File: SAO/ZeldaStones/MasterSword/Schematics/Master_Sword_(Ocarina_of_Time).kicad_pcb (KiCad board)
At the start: 2 copper layers, 99.7 x 99.6 mm, 19 parts, among them J1 Conn_02x03_Odd_Even, J10 USB_B_Micro, J2 Conn_02x03_Odd_Even, J3 Conn_02x03_Odd_Even, J4 Conn_02x03_Odd_Even, SW1 SW_SPDT, U3 HX4056, U4 TLV1117-33

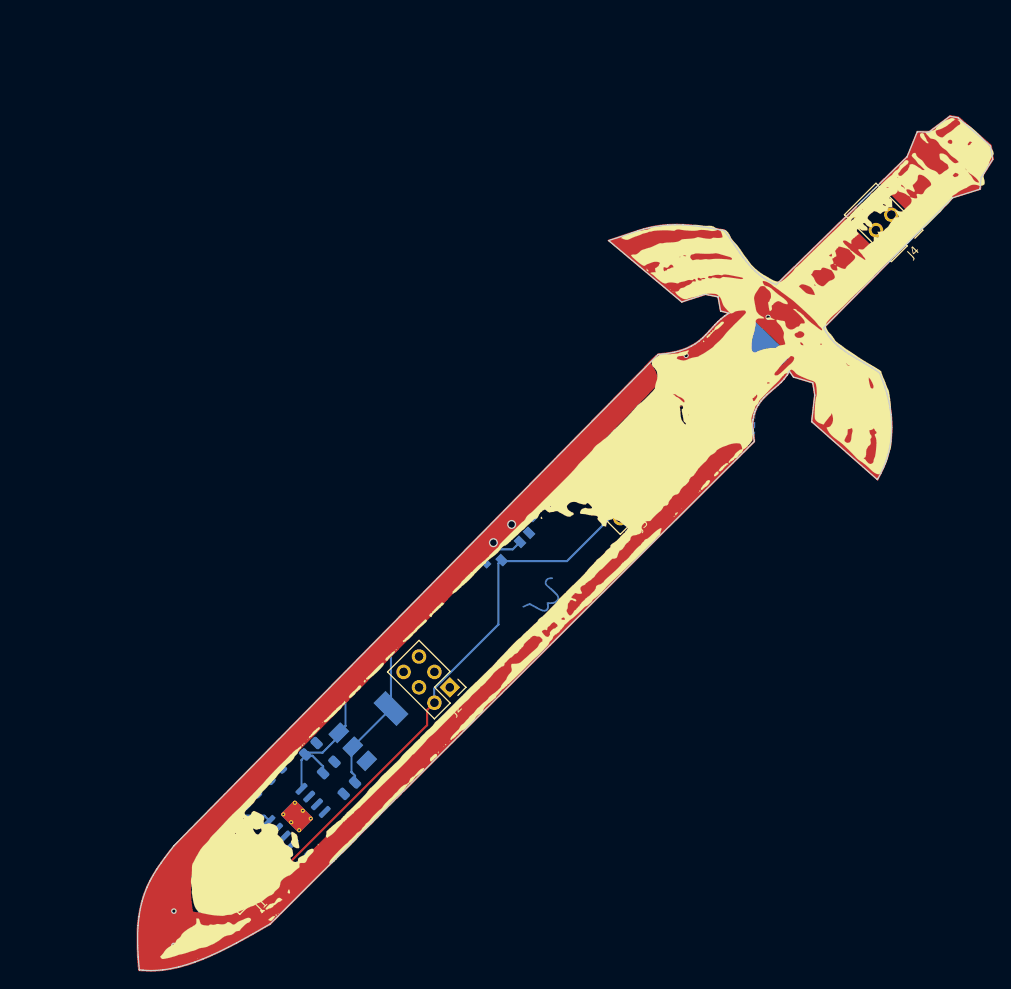
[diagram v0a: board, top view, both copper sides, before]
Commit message: Making stencils
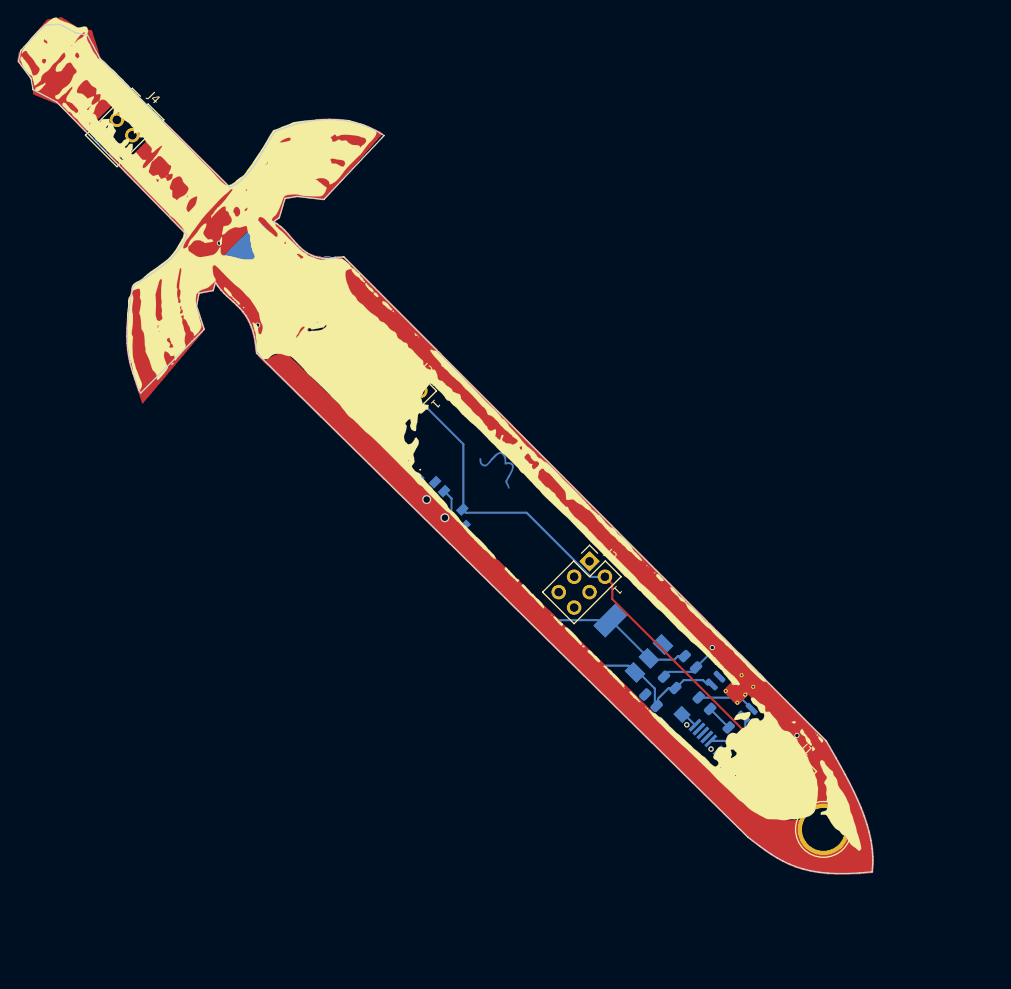
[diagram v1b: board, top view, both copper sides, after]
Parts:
- removed the G*** at (144.3, 104.7) (x3)
- added G*** (x3): LOGO, LOGO, F.Cu at (132.4, 94.6)
- added REF**: TestPoint_Plated_Hole_D5.0mm, TestPoint:TestPoint_Plated_Hole_D5.0mm, F.Cu at (176.0, 137.7)
- <- Power: renamed from SW1
- moved J4 91.4 mm to (95.5, 53.2), turned to 315 degrees
- moved J10 65.2 mm to (160.5, 127.9), turned to 135 degrees
- moved J1 63.5 mm to (171.6, 129.1), turned to 315 degrees
- moved BT1 57.5 mm to (110.7, 71.8), turned to 135 degrees
- moved R2 57.0 mm to (170.3, 125.8), turned to 225 degrees
- moved C14 56.9 mm to (165.7, 126.4), turned to 315 degrees
- moved U3 53.7 mm to (166.2, 121.3), turned to 135 degrees
- moved R5 50.7 mm to (162.2, 123.0), turned to 315 degrees
- moved C18 42.4 mm to (160.5, 118.1), turned to 315 degrees
- moved C16 40.9 mm to (158.1, 120.5), turned to 135 degrees
- moved C17 40.0 mm to (155.9, 122.6), turned to 315 degrees
- moved U4 31.8 mm to (153.5, 115.5), turned to 135 degrees
- moved J3 30.7 mm to (127.3, 84.8), turned to 315 degrees
- moved J2 21.9 mm to (148.8, 106.4), turned to 315 degrees
- moved Ref** 17.5 mm to (139.2, 94.7), turned to 315 degrees
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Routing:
- net VSS: track 43.6 -> 72.4 mm, vias 3 -> 5
- net Net-(C14-Pad2): track 23.9 -> 6.31 mm
- net (no net): track 0.00 -> 5.31 mm
- net Net-(R2-Pad1): track 5.48 -> 3.36 mm
- net Net-(C14-Pad1): track 2.21 -> 3.16 mm
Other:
- board size 99.7 x 99.6 mm -> 99.6 x 99 mm
- board text added: "1"
- board text added: "RMA Badge"
